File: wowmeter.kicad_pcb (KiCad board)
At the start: 2 copper layers, 151.5 x 83.8 mm, 84 parts, among them IC1 LF351, IC2 NE565, IC3 µA747, IC4 LF351, IC5 LF351, IC8 LF351, IC9 LF353, J1 Audio IN, J2 CAL_JMP, J3 AC IN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

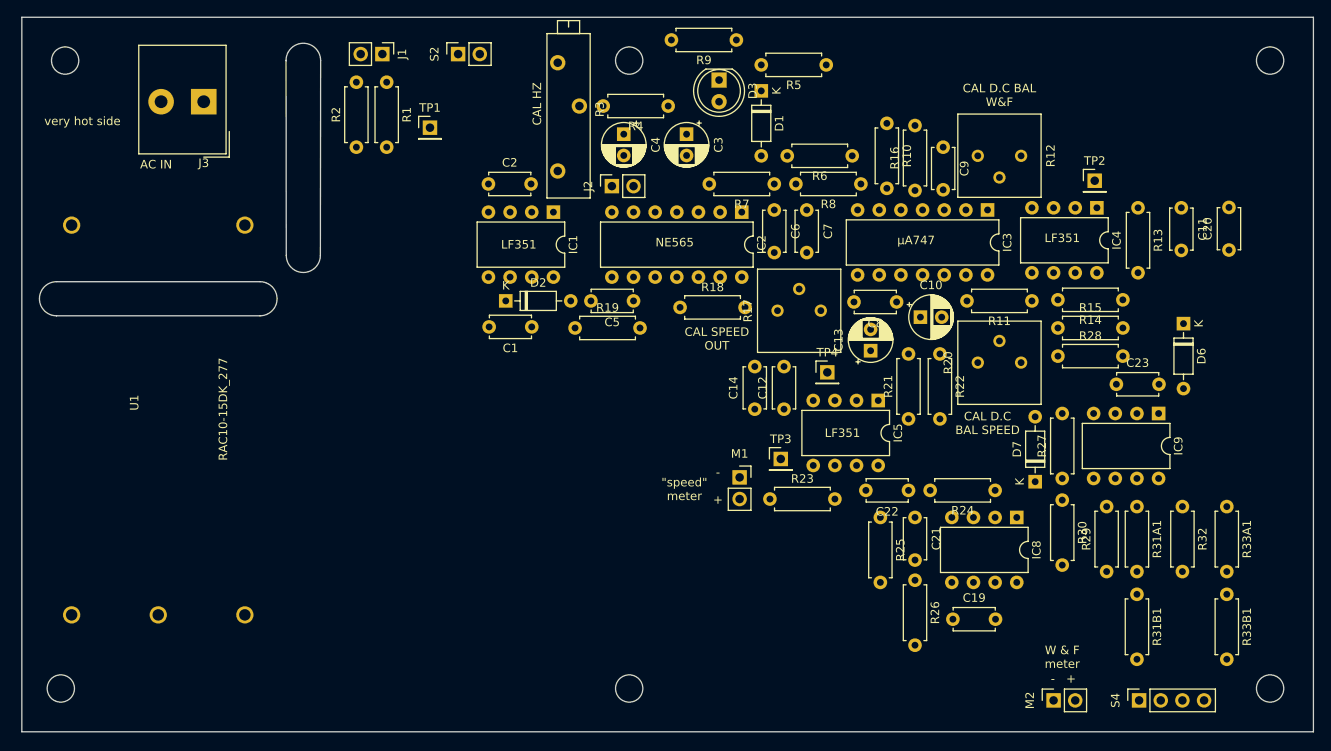
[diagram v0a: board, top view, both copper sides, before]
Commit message: Finished routing the PCB
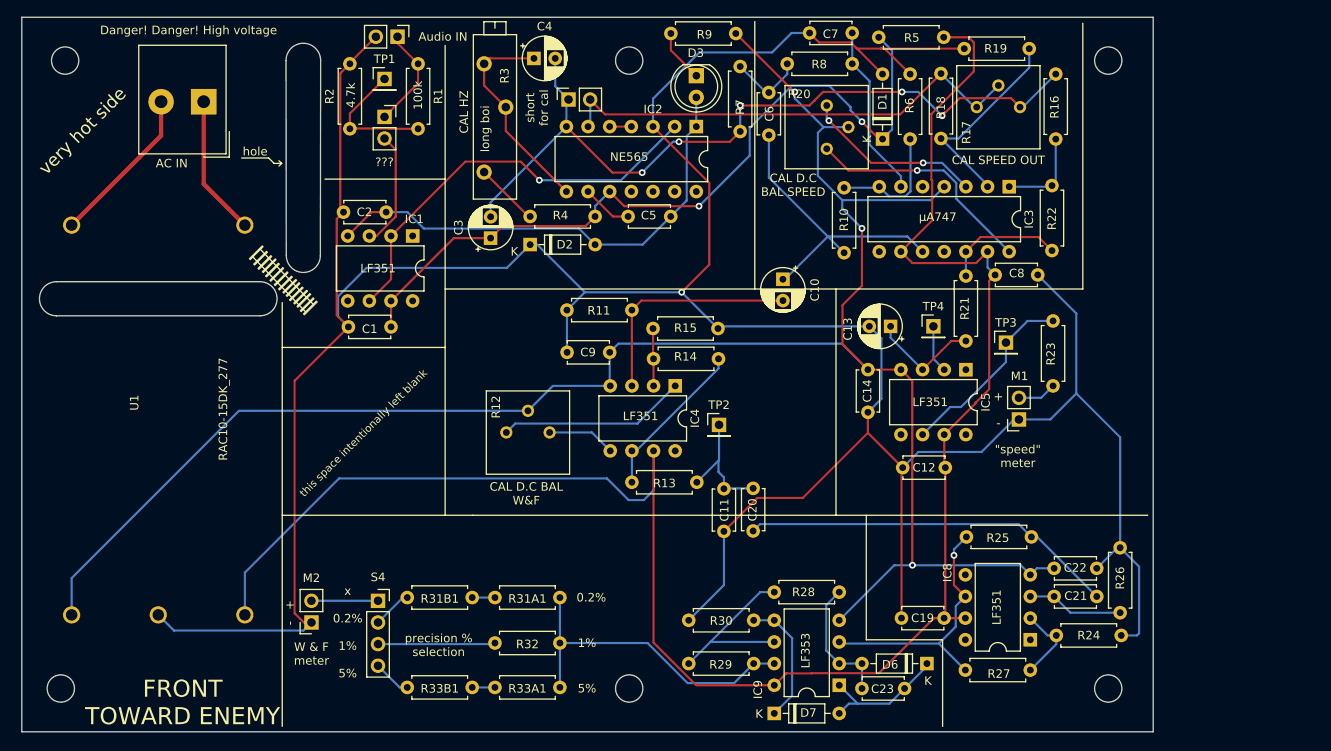
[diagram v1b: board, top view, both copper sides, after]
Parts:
- moved S4 90.0 mm to (69.7, 83.7), turned to 0 degrees
- moved R33B1 89.2 mm to (80.8, 93.9), turned to 180 degrees
- moved M2 87.5 mm to (61.9, 86.2), turned to 180 degrees
- moved R33A1 81.1 mm to (91.1, 93.9), turned to 180 degrees
- moved R31B1 78.0 mm to (80.8, 83.3), turned to 180 degrees
- moved R32 74.8 mm to (91.1, 88.6), turned to 180 degrees
- moved R31A1 68.5 mm to (91.1, 83.3), turned to 180 degrees
- moved C20 64.8 mm to (113.7, 75.5)
- moved C11 63.0 mm to (110.3, 70.5)
- moved R13 60.9 mm to (107.1, 69.8), turned to 180 degrees
- moved R12 59.8 mm to (89.9, 63.9), turned to 90 degrees
- moved R19 56.2 mm to (138.5, 18.9)
- moved R14 55.5 mm to (102.0, 55.3), turned to 0 degrees
- moved IC4 53.7 mm to (104.6, 58.5)
- moved TP2 52.6 mm to (109.7, 63.1)
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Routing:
- net GND: track 0.00 -> 399.8 mm, vias 0 -> 1
- net -15V: track 0.00 -> 232.7 mm, vias 0 -> 3
- net +15V: track 0.00 -> 217.2 mm
- net Net-(C3-Pad2): track 0.00 -> 92.4 mm, vias 0 -> 5
- net Net-(C1-Pad1): track 0.00 -> 91.0 mm, vias 0 -> 2
- net Net-(C2-Pad1): track 0.00 -> 57.2 mm
- net Net-(IC2-Pad6): track 0.00 -> 56.5 mm
- net Net-(IC1-Pad2): track 0.00 -> 49.1 mm, vias 0 -> 1
- net Net-(C20-Pad1): track 0.00 -> 44.2 mm
- net Net-(IC9-Pad7): track 0.00 -> 38.6 mm
- net Net-(C10-Pad1): track 0.00 -> 36.6 mm
- net Net-(IC8-Pad6): track 0.00 -> 31.1 mm, vias 0 -> 1
- net Net-(IC3-Pad14): track 0.00 -> 27.5 mm, vias 0 -> 1
- net Net-(C10-Pad2): track 0.00 -> 27.1 mm
- net Net-(C4-Pad1): track 0.00 -> 25.1 mm
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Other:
- board size 151.5 x 83.8 mm -> 132.7 x 83.8 mm
- board text added: "0.2%"
- board text added: "1%"
- board text added: "5%"
- board text added: "Danger! Danger! High voltage"
- board text added: "FRONT TOWARD ENEMY"
- board text added: "hole"
- board text added: "long boi"
- board text added: "precision % selection"
- board text added: "short for cal"
- board text added: "this space intentionally left blank"
- board text added: "x 0.2% 1% 5%"

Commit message: Ground plane + stitch
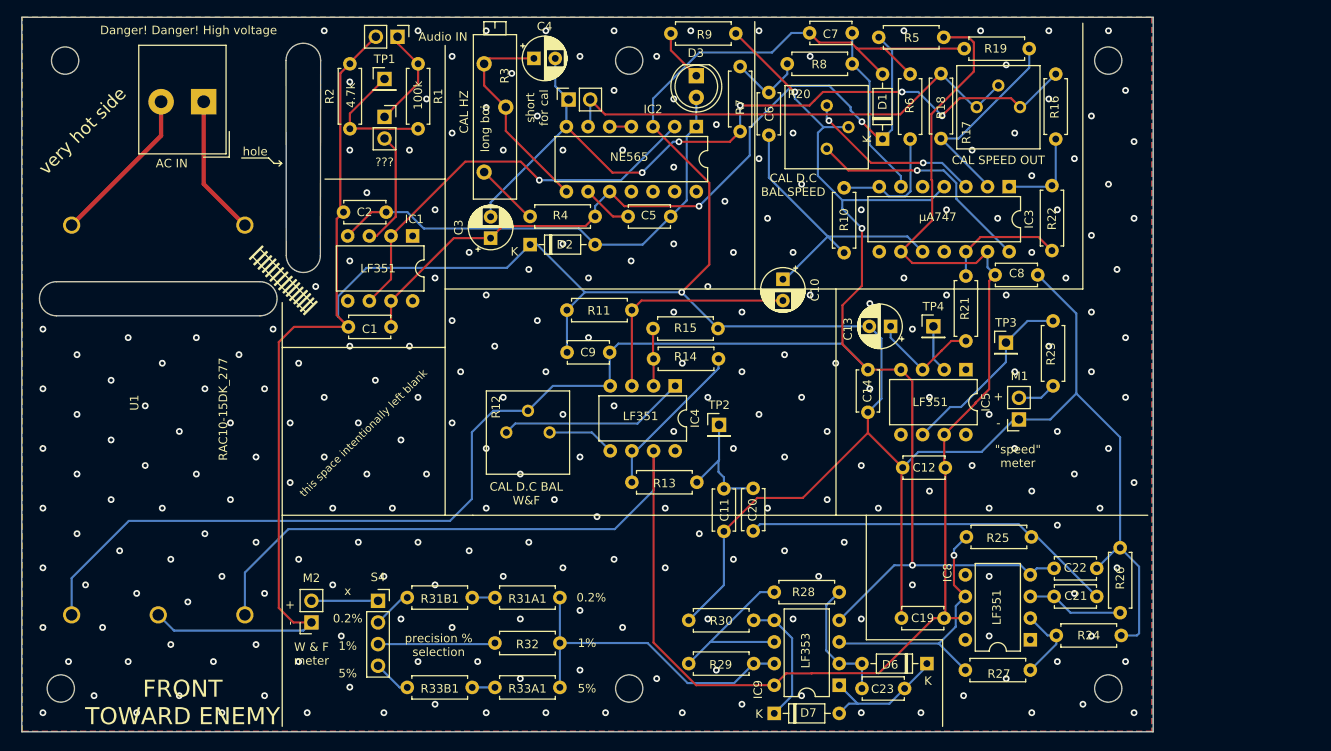
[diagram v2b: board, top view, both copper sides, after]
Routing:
- net GND: track 399.8 -> 405.8 mm, vias 1 -> 252
- net -15V: track 232.7 -> 237.3 mm
- net +15V: track 217.2 -> 215.1 mm
- added copper zone on B.Cu, net GND
- added copper zone on F.Cu, net GND
